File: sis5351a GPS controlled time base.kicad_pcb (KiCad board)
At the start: 2 copper layers, 90.9 x 82.5 mm, 52 parts, among them J1 USB_B_Micro, J2 Conn_01x05_Pin, J3 Conn_01x04_Pin, J4 Conn_02x03_Odd_Even, J5 Conn_01x12_Pin, J6 Conn_Coaxial, J7 Conn_Coaxial, Q1 BSS138, Q2 BSS138, U1 Si5351A-B-GT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

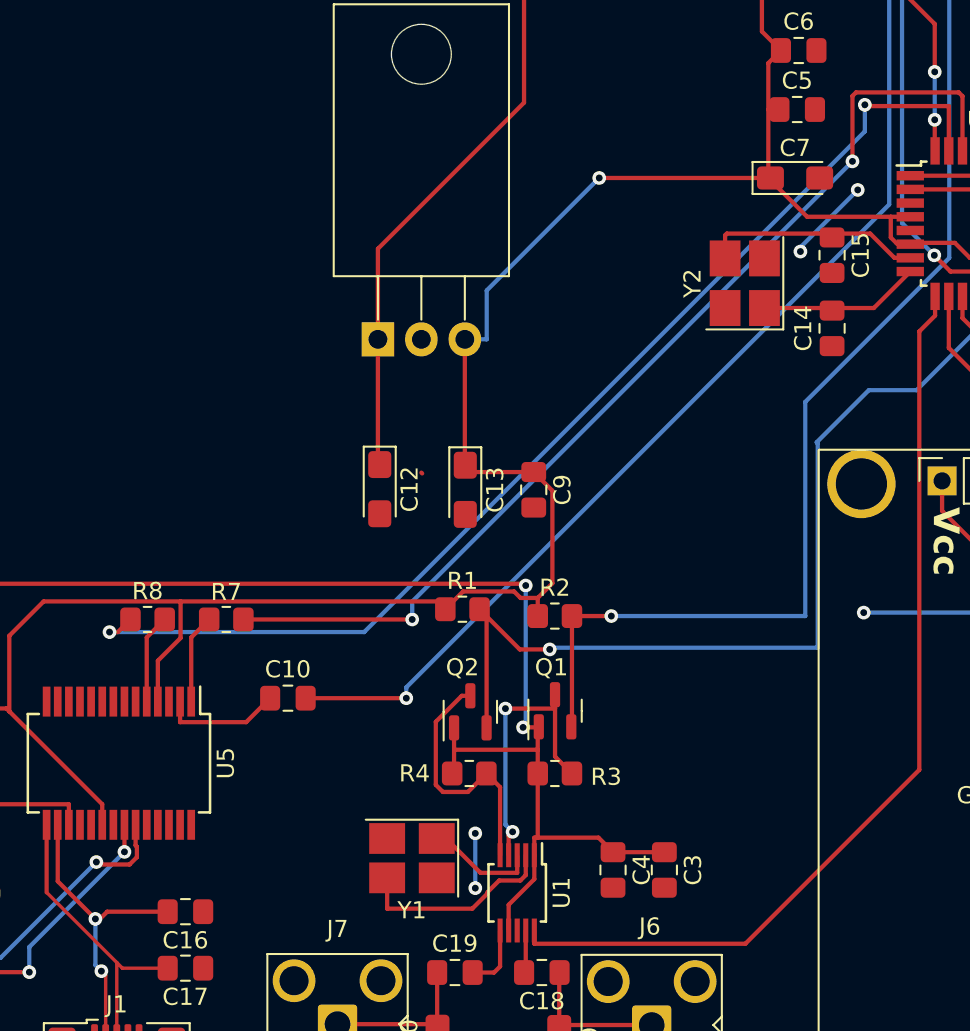
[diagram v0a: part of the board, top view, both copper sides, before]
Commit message: Fault in I2C level converter
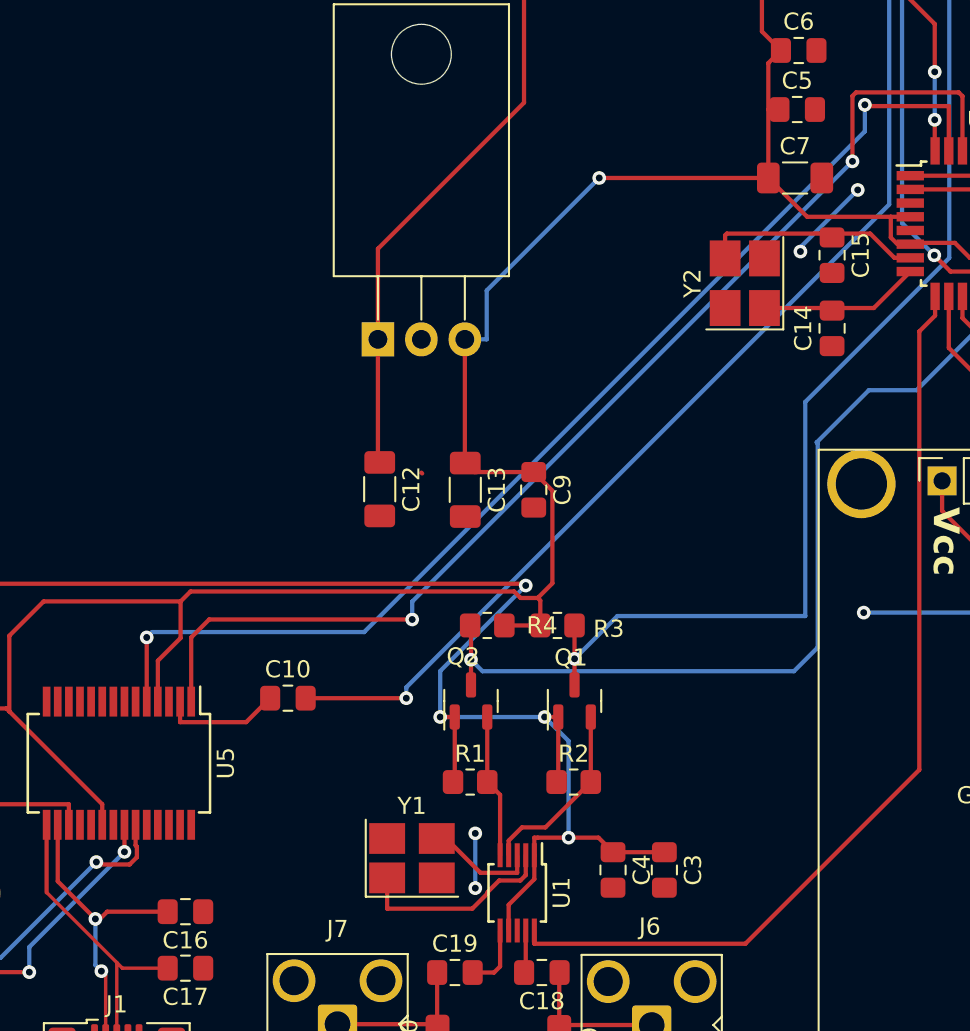
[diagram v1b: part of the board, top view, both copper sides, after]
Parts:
- removed R7, R8: 1K, Resistor_SMD:R_0805_2012Metric_Pad1.20x1.40mm_HandSolder
- C12, C13, C7: footprint Capacitor_Tantalum_SMD:CP_EIA-3216-10_Kemet-I_Pad1.58x1.35mm_HandSolder -> Capacitor_SMD:C_1206_3216Metric_Pad1.33x1.80mm_HandSolder
- moved R1 10.1 mm to (163.4, 117.9)
- moved R2 9.76 mm to (169.5, 117.9)
- moved R4 8.71 mm to (164.4, 108.8), turned to 180 degrees
- moved R3 8.65 mm to (168.6, 108.8)
- moved Q1 1.27 mm to (169.6, 113.2)
- moved Q2 0.64 mm to (163.5, 113.2)
- turned Y1 to 0 degrees
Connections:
- Q1 pad 2: SCL5 -> SCL3
- Q1 pad 3: SCL3 -> SCL5
- Q2 pad 2: SDA5 -> SDA3
- Q2 pad 3: SDA3 -> SDA5
- R1 pad 1: +5V -> +3V3
- R1 pad 2: SDA5 -> SDA3
- R2 pad 1: +5V -> +3V3
- R2 pad 2: SCL5 -> SCL3
- R3 pad 1: +3V3 -> +5V
- R3 pad 2: SCL3 -> SCL5
- R4 pad 1: +3V3 -> +5V
- R4 pad 2: SDA3 -> SDA5
- U5 pad 1: Net-(U5-TXD) -> USB_RXD
- U5 pad 5: Net-(U5-RXD) -> USB_TXD
- Y1 pad 1: Net-(U1-XB) -> Net-(U1-XA)
- Y1 pad 3: Net-(U1-XA) -> Net-(U1-XB)
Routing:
- net +3V3: track 91.0 -> 100.4 mm, vias 2 -> 4
- net USB_RXD: track 60.9 -> 68.2 mm
- net SDA3: track 15.0 -> 8.39 mm
- net SCL3: track 16.7 -> 10.9 mm, vias 2 -> 0
- net Net-(U5-TXD): track 5.23 -> 0.00 mm
- net Net-(U5-RXD): track 5.23 -> 0.00 mm
- net SDA5: track 100.3 -> 97.0 mm
- net +5V: track 291.4 -> 293.7 mm
- net SCL5: track 87.6 -> 85.4 mm
